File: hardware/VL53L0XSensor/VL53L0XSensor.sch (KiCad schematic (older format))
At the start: 14 parts, among them J1 Conn_01x03_Male, J2 Conn_01x04_Female, J3 Conn_01x02_Male, J4 Conn_01x03_Male, SW1 SW_SPDT, U1 ATtiny3216-S

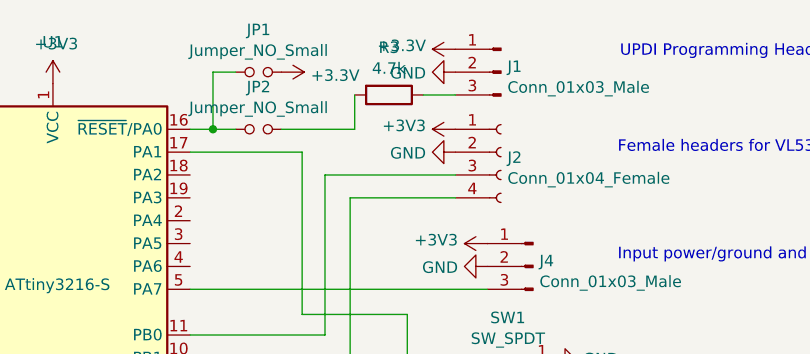
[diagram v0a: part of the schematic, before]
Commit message: vl53l0x sensor pcb updates and pot pcb updates
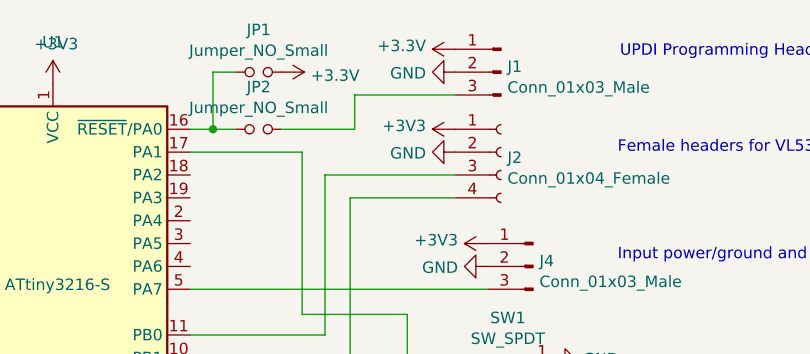
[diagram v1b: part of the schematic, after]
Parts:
- removed R3: 4.7k, Resistor_SMD:R_1206_3216Metric, symbol Device:R
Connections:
- net at JP2.2: now also J1.3 (Pin_3)
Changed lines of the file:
@@
-$EndComp
-$Comp
-L Device:R R3
-U 1 1 5F0EEFFE
-P 6310 3080
-F 0 "R3" V 6103 3080 50  0000 C CNN
-F 1 "4.7k" V 6194 3080 50  0000 C CNN
-F 2 "Resistor_SMD:R_1206_3216Metric" V 6240 3080 50  0001 C CNN
-F 3 "~" H 6310 3080 50  0001 C CNN
-	1    6310 3080
-	0    1    1    0
 $EndComp
 $Comp
@@
 	0    1    1    0
 $EndComp
-Wire Wire Line
-	6600 3080 6460 3080
 Wire Wire Line
 	6160 3080 6160 3230
@@
 Wire Wire Line
 	5440 4540 5440 4530
+Wire Wire Line
+	6160 3080 6600 3080
 $EndSCHEMATC
